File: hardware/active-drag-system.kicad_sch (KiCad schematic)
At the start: 15 parts, among them J1 Conn_01x02_Pin, J2 Conn_01x02_Socket, J3 10118193-0001LF, J4 Conn_01x05_Pin, J5 Conn_01x02_Pin, J6 Conn_01x02_Pin, J7 Conn_01x03_Pin, J8 Conn_01x03_Pin

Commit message: Added digikey part numbers; usb trace width update
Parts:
- BZ1, J1, J4, J5, J6, J8: now left out of the parts list
- R1: Digikey Part Number (none) -> P100HCT-ND
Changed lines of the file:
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@@
 		(unit 1)
 		(exclude_from_sim no)
-		(in_bom yes)
+		(in_bom no)
 		(on_board yes)
 		(dnp no)
@@
 			)
 		)
+		(property "Digikey Part Number" "P100HCT-ND"
+			(at 102.87 71.12 90)
+			(effects
+				(font
+					(size 1.27 1.27)
+				)
+				(hide yes)
+			)
+		)
 		(pin "2"
 		)
@@
 		(unit 1)
 		(exclude_from_sim no)
-		(in_bom yes)
+		(in_bom no)
 		(on_board yes)
 		(dnp no)
@@
 		(unit 1)
 		(exclude_from_sim no)
-		(in_bom yes)
+		(in_bom no)
 		(on_board yes)
 		(dnp no)
@@
 		(unit 1)
 		(exclude_from_sim no)
-		(in_bom yes)
+		(in_bom no)
 		(on_board yes)
 		(dnp no)
@@
 		(unit 1)
 		(exclude_from_sim no)
-		(in_bom yes)
+		(in_bom no)
 		(on_board yes)
 		(dnp no)
@@
 		(unit 1)
 		(exclude_from_sim no)
-		(in_bom yes)
-		(on_board yes)
-		(dnp no)
+		(in_bom no)
+		(on_board yes)
+		(dnp no)

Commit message: Rev 2
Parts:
- removed J6: Conn_01x02_Pin, Connector_PinHeader_2.54mm:PinHeader_1x02_P2.54mm_Vertical, symbol Connector:Conn_01x02_Pin
- added J6: Conn_01x04_Pin, Connector_PinHeader_2.54mm:PinHeader_1x04_P2.54mm_Vertical, symbol Connector:Conn_01x04_Pin
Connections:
- net +3V3: now also J6.1 (Pin_1)
- net GND: now also J6.2 (Pin_2)
- net MCU_RP2040/I2C1_SCL: now also J6.3 (Pin_3)
- net MCU_RP2040/I2C1_SDA: now also J6.4 (Pin_4)

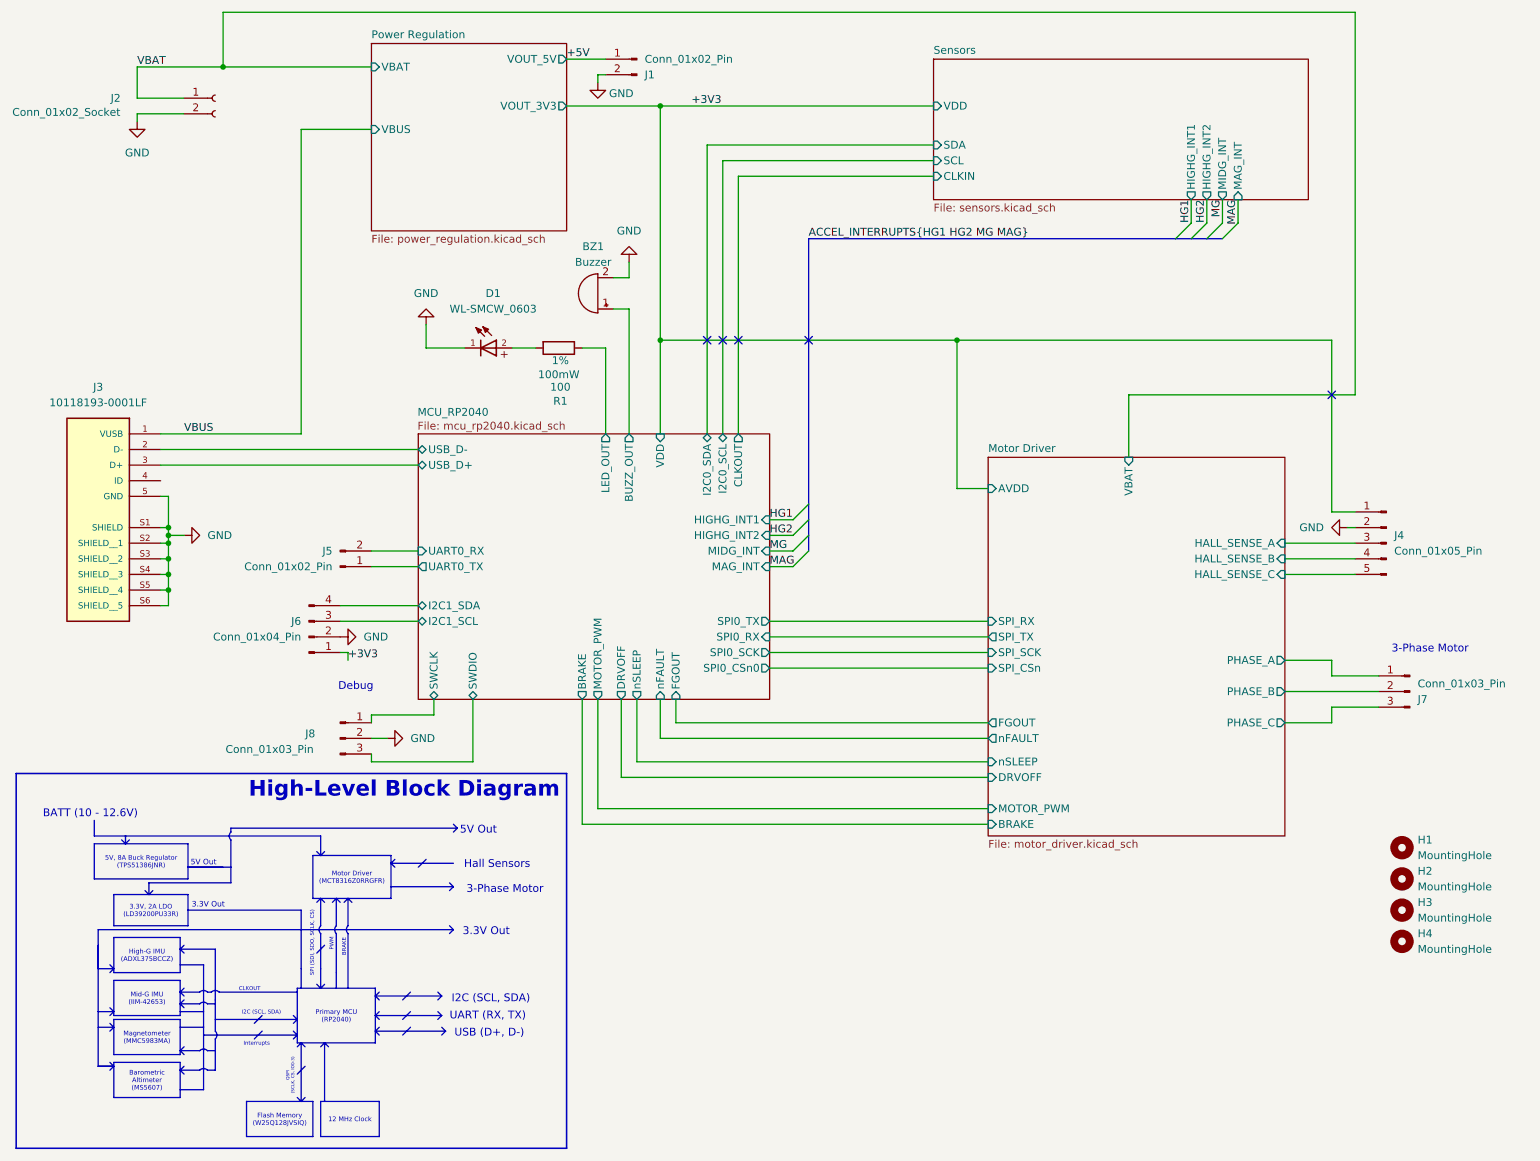
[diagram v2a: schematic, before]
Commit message: version of pcb with no motor driver, only previously used servo enable and pwm circuit
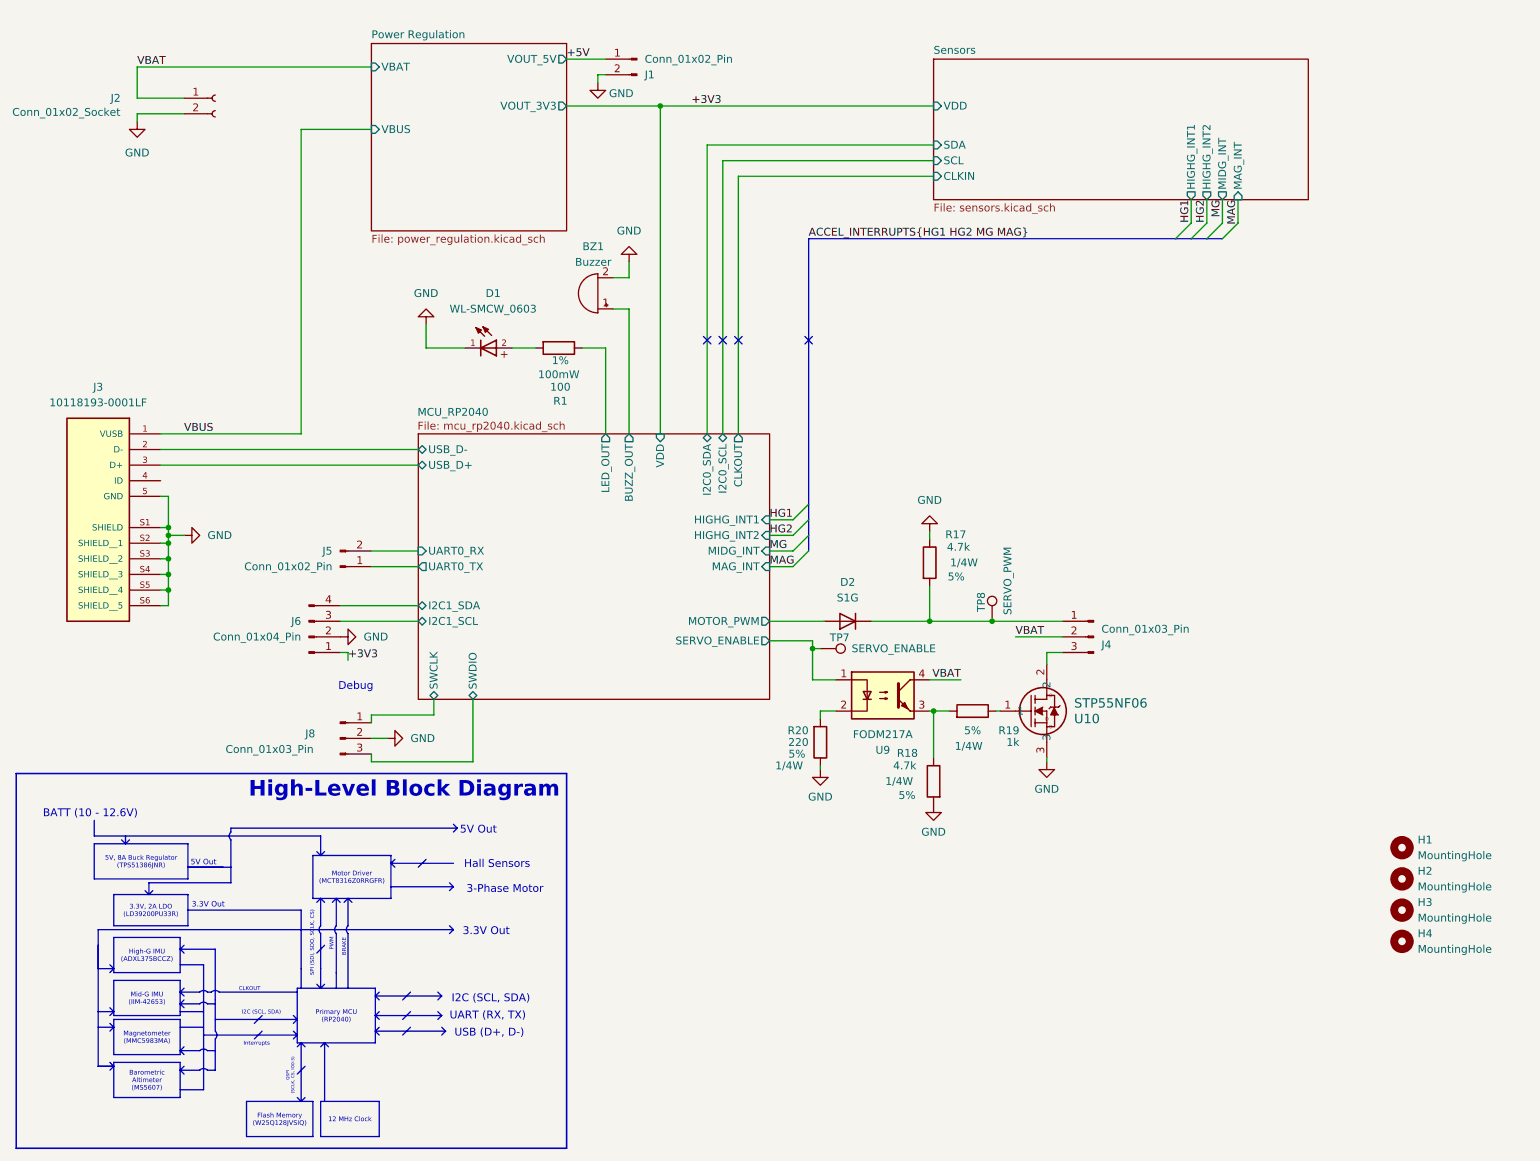
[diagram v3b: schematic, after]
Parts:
- removed J4: Conn_01x05_Pin, Connector_PinHeader_2.54mm:PinHeader_1x05_P2.54mm_Vertical, symbol Connector:Conn_01x05_Pin
- removed J7: Conn_01x03_Pin, active-drag-system:SolderWire-2sqmm_1x03_P7.8mm_D2mm_OD3.9mm, symbol Connector:Conn_01x03_Pin
- added D2: S1G, Diode_SMD:D_SMA, symbol Device:D
- added J4: Conn_01x03_Pin, Connector_PinHeader_2.54mm:PinHeader_1x03_P2.54mm_Vertical, symbol Connector:Conn_01x03_Pin
- added R17, R18: 4.7k, Resistor_SMD:R_1206_3216Metric, symbol Device:R
- added R19: 1k, Resistor_SMD:R_1206_3216Metric, symbol Device:R
- added R20: 220, Resistor_SMD:R_1206_3216Metric, symbol Device:R
- added TP7: SERVO_ENABLE, TestPoint:TestPoint_Pad_1.0x1.0mm, symbol Connector:TestPoint
- added TP8: SERVO_PWM, TestPoint:TestPoint_Pad_1.0x1.0mm, symbol Connector:TestPoint
- added U10: STP55NF06, active-drag-system:STP55NF06, symbol active-drag-system:STP55NF06
- added U9: FODM217A, Package_SO:SOP-4_4.4x2.6mm_P1.27mm, symbol Isolator:FODM217A
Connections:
- net GND: now also R17.1, R18.2, R20.1, U10.3
- net MCU_RP2040/MOTOR_PWM: now also D2.2 (A)
- net VBAT: now also J4.2 (Pin_2), U9.4
- new net: D2.1 (K), J4.1 (Pin_1), R17.2, TP8.1
- new net: J4.3 (Pin_3), U10.2
- new net: R19.1, U10.1
- new net: R18.1, R19.2, U9.3
- new net: R20.2, U9.2
- new net MCU_RP2040/SERVO_ENABLE: TP7.1, U9.1
- no-connect marks 5 -> 4
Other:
- removed sheet Motor Driver
- sheet MCU_RP2040 ports: added SERVO_ENABLE; removed BRAKE, DRVOFF, FGOUT, SPI0_CSn0, SPI0_RX, SPI0_SCK, SPI0_TX, nFAULT, nSLEEP
